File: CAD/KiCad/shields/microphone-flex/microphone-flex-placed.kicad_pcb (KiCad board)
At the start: 2 copper layers, 32 x 62 mm, 22 parts, among them J1 GND / +5V / OUT, J2 LEFT / 1x05 RIGHT ANGLE, J3 RIGHT / 1x05 RIGHT ANGLE, M1 UP / ONE MODULE ONLY

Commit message: Restore removable microphone gain and A/R selectors across flex design
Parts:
- removed R1: 0R / GAIN VDD 40dB, Shields:R_0603_1608Metric
- removed R2: 0R / AR GND 1:500, Shields:R_0603_1608Metric
- added JP1: GAIN SELECT / HEADER + SHUNT, Shields:Flex_Gain_Selector, F.Cu at (51.2, 88.0)
- added JP2: AR SELECT / HEADER + SHUNT, Shields:Flex_AR_Selector, F.Cu at (68.8, 88.0)
- moved C6 1.50 mm to (68.0, 96.5)
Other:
- board text added: "50/60/40"
- board text added: "500/4K/2K"
- board text added: "COLLOQUY MIC C-J"
- board text added: "JP1 GAIN"
- board text added: "JP2 A/R"
- board text removed: "COLLOQUY MIC C"

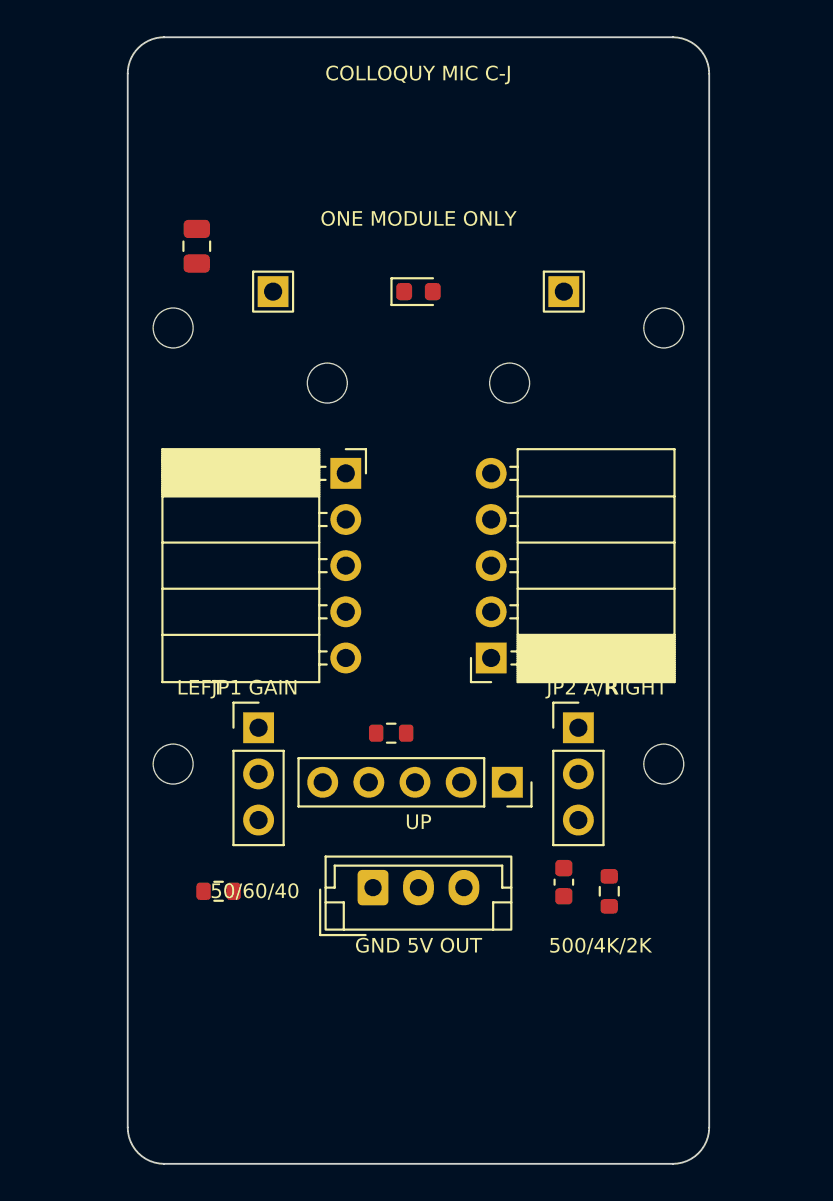
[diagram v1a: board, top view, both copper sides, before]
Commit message: Reroute microphone flex around the approved component placement
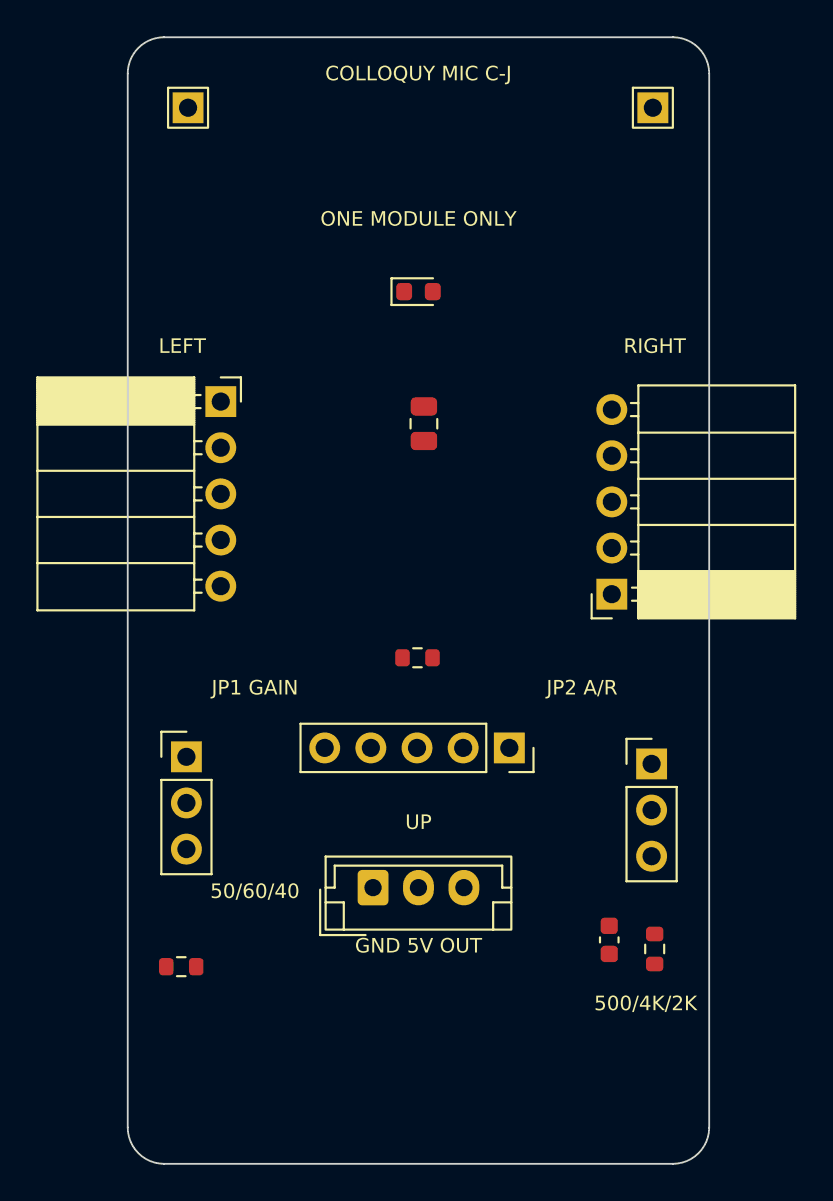
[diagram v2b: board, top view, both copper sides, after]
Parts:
- removed H3, H4: M2 MODULE / INSULATING SPACER, Shields:Flex_M2_Top
- removed H5, H6, H7, H8: M2 SIDE SUPPORT BASE, Shields:Flex_M2_Base
- moved C7 15.9 mm to (60.3, 71.3)
- moved TP1 11.2 mm to (72.9, 53.9)
- moved TP2 11.1 mm to (47.3, 53.9)
- moved J2 7.93 mm to (49.1, 70.0)
- moved J3 7.51 mm to (70.6, 80.7)
- moved R4 4.63 mm to (46.9, 101.2)
- moved JP2 4.49 mm to (72.8, 90.0)
- moved R5 4.39 mm to (59.9, 84.2)
- moved JP1 4.28 mm to (47.2, 89.6)
- moved C6 4.04 mm to (70.5, 99.7)
- moved R6 4.04 mm to (73.0, 100.2)
- moved M1 1.90 mm to (65.0, 89.1)

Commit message: Flip side microphones below the carrier and reverse their pin mapping
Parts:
- J2: value LEFT / 1x05 RIGHT ANGLE -> LEFT / DOWNWARD MODULE
- J3: value RIGHT / 1x05 RIGHT ANGLE -> RIGHT / DOWNWARD MODULE
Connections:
- J2 pad 1: AR -> GND
- J2 pad 2: MICOUT -> VDD
- J2 pad 4: VDD -> MICOUT
- J2 pad 5: GND -> AR
- J3 pad 1: AR -> GND
- J3 pad 2: MICOUT -> VDD
- J3 pad 4: VDD -> MICOUT
- J3 pad 5: GND -> AR
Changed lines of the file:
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@@
 			)
 		)
-		(property "Value" "LEFT / 1x05 RIGHT ANGLE"
+		(property "Value" "LEFT / DOWNWARD MODULE"
 			(at -4.38 12.93 0)
 			(layer "F.Fab")
@@
 			(layers "*.Cu" "*.Mask")
 			(remove_unused_layers no)
-			(net 2 "AR")
+			(net 4 "GND")
 		)
 		(pad "2" thru_hole circle
@@
 			(layers "*.Cu" "*.Mask")
 			(remove_unused_layers no)
-			(net 5 "MICOUT")
+			(net 7 "VDD")
 		)
 		(pad "3" thru_hole circle
@@
 			(layers "*.Cu" "*.Mask")
 			(remove_unused_layers no)
-			(net 7 "VDD")
+			(net 5 "MICOUT")
 		)
 		(pad "5" thru_hole circle
@@
 			(layers "*.Cu" "*.Mask")
 			(remove_unused_layers no)
-			(net 4 "GND")
+			(net 2 "AR")
 		)
 		(embedded_fonts no)
@@
 			)
 		)
-		(property "Value" "RIGHT / 1x05 RIGHT ANGLE"
+		(property "Value" "RIGHT / DOWNWARD MODULE"
 			(at -4.38 12.93 180)
 			(layer "F.Fab")
@@
 			(layers "*.Cu" "*.Mask")
 			(remove_unused_layers no)
-			(net 2 "AR")
+			(net 4 "GND")
 		)
 		(pad "2" thru_hole circle
@@
 			(layers "*.Cu" "*.Mask")
 			(remove_unused_layers no)
-			(net 5 "MICOUT")
+			(net 7 "VDD")
 		)
 		(pad "3" thru_hole circle
@@
 			(layers "*.Cu" "*.Mask")
 			(remove_unused_layers no)
-			(net 7 "VDD")
+			(net 5 "MICOUT")
 		)
 		(pad "5" thru_hole circle
@@
 			(layers "*.Cu" "*.Mask")
 			(remove_unused_layers no)
-			(net 4 "GND")
+			(net 2 "AR")
 		)
 		(embedded_fonts no)
